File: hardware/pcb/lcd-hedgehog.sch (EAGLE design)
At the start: 22 parts

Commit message: added ble
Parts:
- added U$6: BLE113-A, jnode:BLE113-A
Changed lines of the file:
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@@
 <part name="U$4" library="HedgehogLib" deviceset="SFV23" device=""/>
 <part name="U$5" library="HedgehogLib" deviceset="LM2703" device=""/>
+<part name="U$6" library="jnode" deviceset="BLE113-A" device=""/>
 </parts>
 <sheets>
@@
 <instance part="U$4" gate="G$1" x="233.68" y="180.34"/>
 <instance part="U$5" gate="G$1" x="233.68" y="223.52"/>
+<instance part="U$6" gate="G$1" x="76.2" y="172.72"/>
 </instances>
 <busses>

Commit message: added some wiring
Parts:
- removed C_UC_P28/29, C_UC_P7/8: 0.22u, rcl:C-EUC0603K
- removed U$2: LSM303LGA28_LONG, jnode:LSM303LGA28_LONG
- added CC_DEBUGER: PROGCON, HedgehogLib:PROGCON
- added C_PWR_SW1, C_PWR_SW2: 10u, rcl:C-EUC0805K
- added HWB, RESET: (no value), jumper:SJ
- added R1: 10k, rcl:R-EU_R0603
- added R5, R6: 22, rcl:R-EU_R0603
- added U$7: LSM9D, jnode:LSM9D
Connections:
- removed net USB_D+@RC5: USB_CON.3
- removed net USB_D-@RC4: USB_CON.2
- new net BLE_RESET: CC_DEBUGER-2.S, U$6.RESET#
- new net CS_SD: U$1.(PCINT4/ADC11)PB4
- new net D+: R5.2, USB_CON.3
- new net D-: R6.2, USB_CON.2
- new net MISO: U$1.(PDO/PCINT3/MISO)PB3
- new net MOSI: U$1.(PDI/PCINT2/MOSI)PB2
- new net N$1: R1.1, RESET.2, U$1.RESET
- new net N$11: U$1.(PCINT6/OC1B/OC4B/ADC13)PB6
- new net N$2: 12MHZ_RESONATOR.2, U$1.XTAL1
- new net N$3: 12MHZ_RESONATOR.1, U$1.XTAL2
- new net N$4: HWB.1, U$1.(HWB)PE2
- new net N$5: R6.1, U$1.D-
- new net N$6: R5.1, U$1.D+
- new net N$7: U$7.SDA
- new net P0_1/INT: U$1.(PCINT5/OC1A/OC4B/ADC12)PB5, U$6.P0_1
- new net P0_4/TX: U$1.(RXD1/INT2)PD2, U$6.P0_4
- new net P0_5/RX: U$1.(TXD1/INT3)PD3, U$6.P0_5
- new net P2_1: CC_DEBUGER-4.S, U$6.P2_1
- new net P2_2: CC_DEBUGER-3.S, U$6.P2_2
- new net SCL: U$1.(OSC0B/SCL/INT0)PD0, U$3.SCL
- new net SDA: U$1.(SDA/INT1)PD1, U$3.SDA
- net +3V3: now also CC_DEBUGER-1.S, C_PWR_SW1.2, C_PWR_SW2.2, R1.2, U$1.AVCC, U$1.AVCC2, U$1.VCC, U$1.VCC2, U$3.VCC, U$6.AVDD, U$6.DVDD; no longer C_UC_P28/29.1, C_UC_P7/8.1
- net GND: now also CC_DEBUGER-5.S, C_PWR_SW1.1, C_PWR_SW2.1, HWB.2, RESET.1, U$1.GND, U$1.GND2, U$1.GND3, U$1.GND4, U$1.GND5, U$1.UCAP, U$1.UGND, U$3.VSS, U$4.VSS, U$5.GND, U$6.GND@1, U$6.GND@10, U$6.GND@11, U$6.GND@2, U$6.GND@3, U$6.GND@4, U$6.GND@5, U$6.GND@6, U$6.GND@8, U$6.GND@9, U$7.GND@1; no longer C_UC_P28/29.2, C_UC_P7/8.2
- net SCLK: now also U$1.(PCINT1/SCLK)PB1
- net V_USB: now also U$1.UVCC, U$1.VBUS
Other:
- note added: "I²C"
- note removed: "pin28&29"
- note removed: "pin37"
- note removed: "pin7&8"
- moved on the sheet: C_UC_P37, U$1

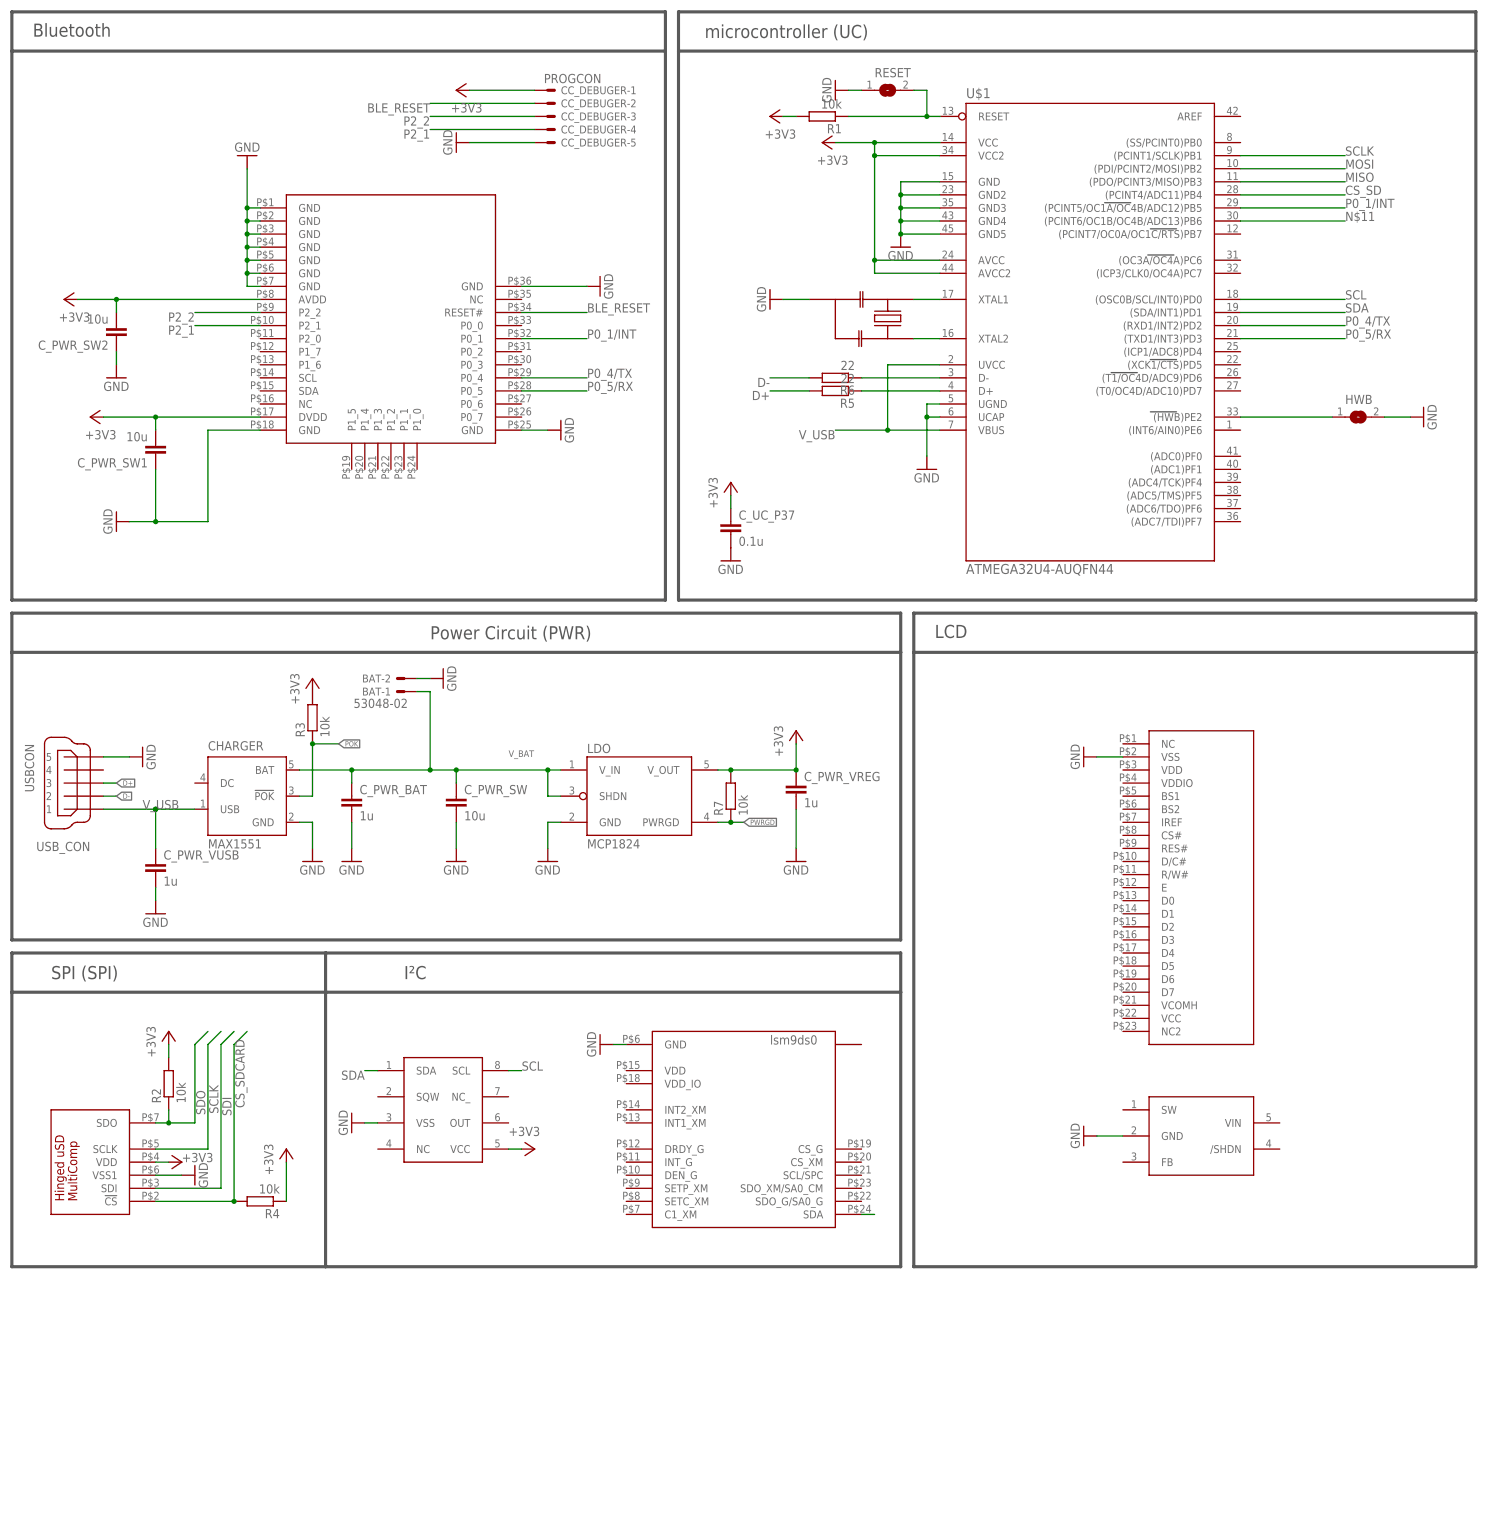
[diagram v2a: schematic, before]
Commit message: connected IMU
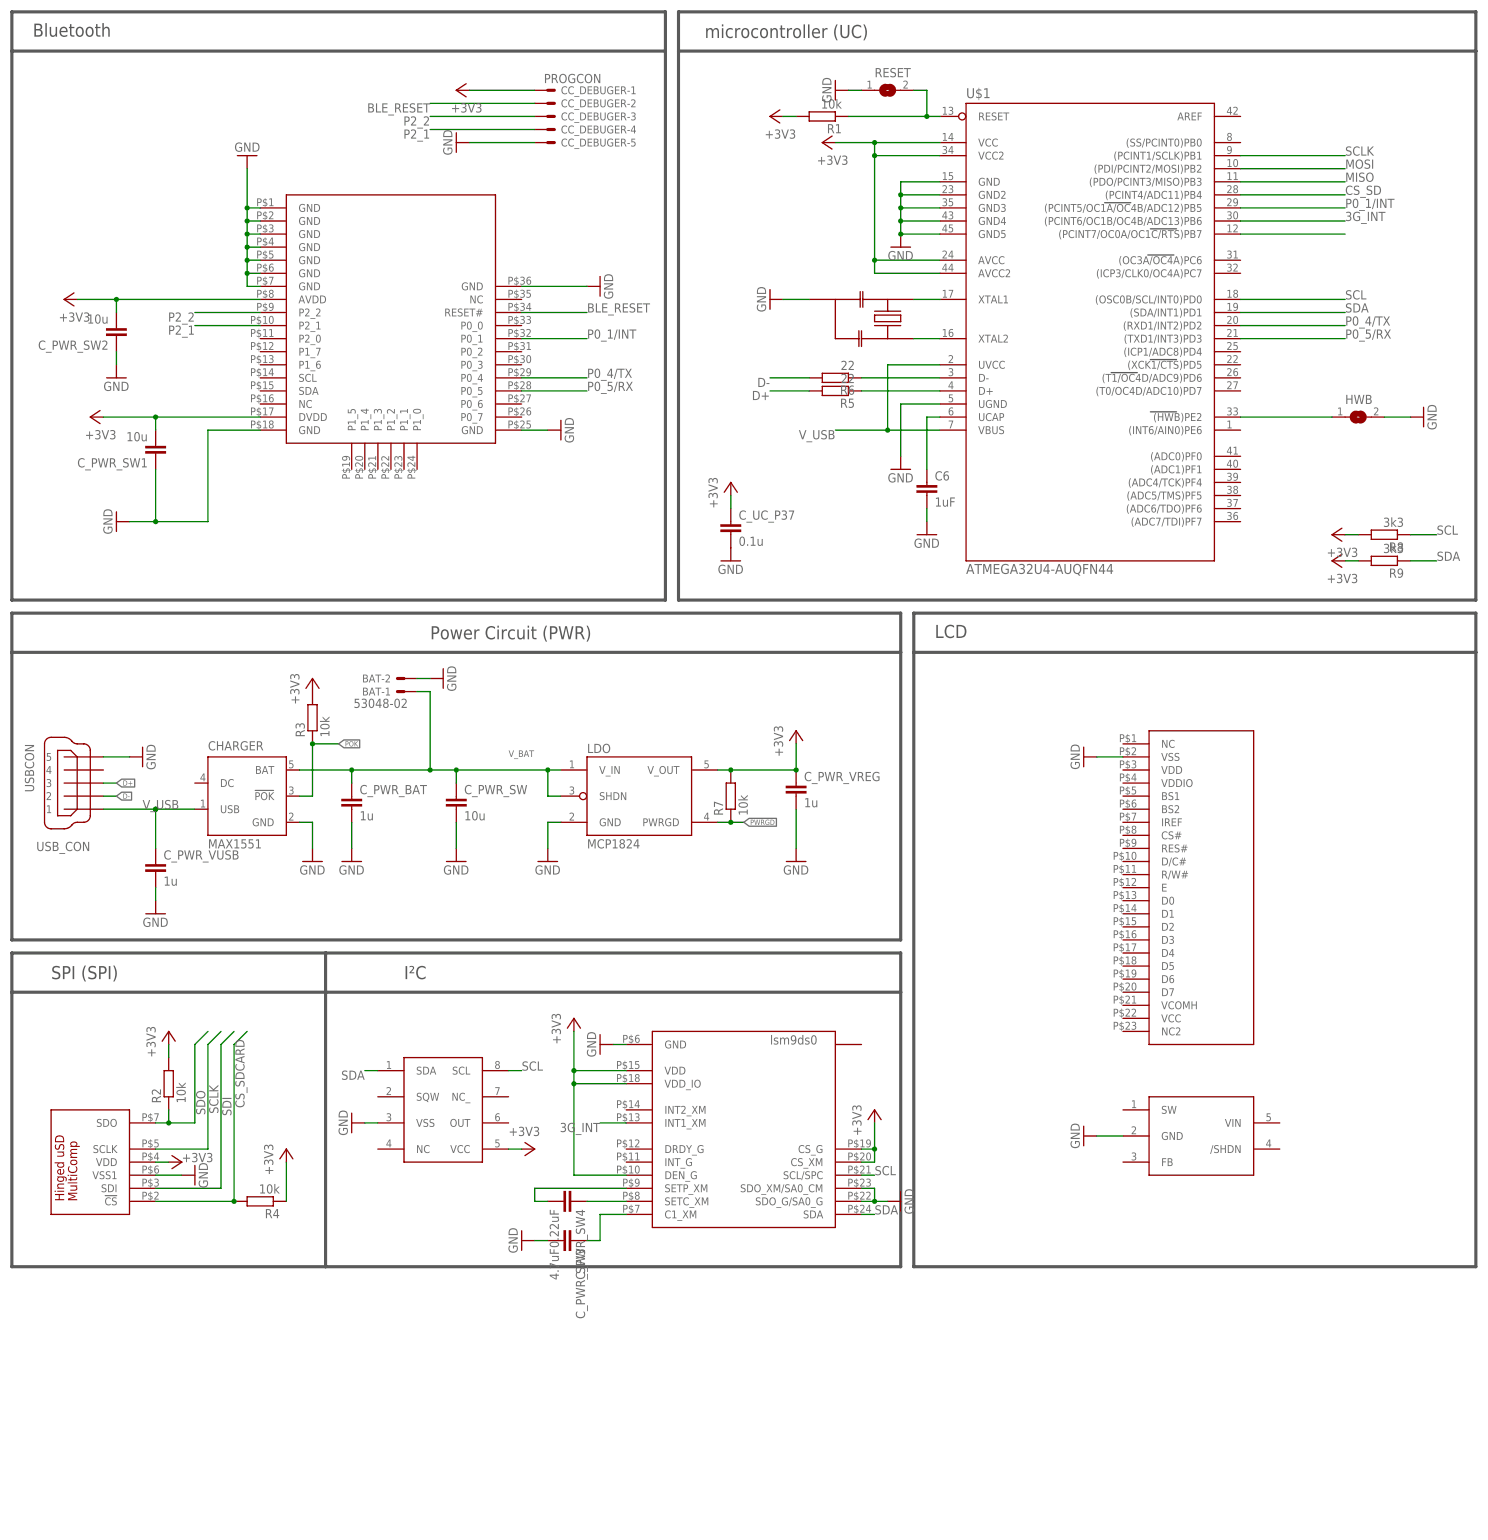
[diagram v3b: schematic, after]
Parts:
- added C6: 1uF, rcl:C-EUC0603K
- added C_PWR_SW3: 4.7uF, rcl:C-EUC0805K
- added C_PWR_SW4: 0.22uF, rcl:C-EUC0805K
- added R8, R9: 3k3, rcl:R-EU_R0603
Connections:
- new net 3G_INT: U$1.(PCINT6/OC1B/OC4B/ADC13)PB6, U$7.INT1_XM
- new net N$10: U$1.(PCINT7/OC0A/OC1C/RTS)PB7
- new net N$8: C_PWR_SW4.2, U$7.SETP_XM
- new net N$9: C_PWR_SW3.1, U$7.C1_XM
- net +3V3: now also R8.2, R9.2, U$7.CS_G, U$7.CS_XM, U$7.DEN_G, U$7.VDD, U$7.VDD_IO
- net GND: now also C6.2, C_PWR_SW3.2, U$7.SDO_G/SA0_G, U$7.SDO_XM/SA0_CM; no longer U$1.UCAP
- net N$11: now also C6.1, U$1.UCAP; no longer U$1.(PCINT6/OC1B/OC4B/ADC13)PB6
- net N$7: now also C_PWR_SW4.1, U$7.SETC_XM; no longer U$7.SDA
- net SCL: now also R8.1, U$7.SCL/SPC
- net SDA: now also R9.1, U$7.SDA
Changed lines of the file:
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@@
 <part name="+3V9" library="supply1" deviceset="+3V3" device=""/>
 <part name="GND18" library="supply1" deviceset="GND" device=""/>
+<part name="+3V12" library="supply1" deviceset="+3V3" device=""/>
+<part name="+3V13" library="supply1" deviceset="+3V3" device=""/>
+<part name="GND19" library="supply1" deviceset="GND" device=""/>
+<part name="C_PWR_SW3" library="rcl" deviceset="C-EU" device="C0805K" value="4.7uF"/>
+<part name="C_PWR_SW4" library="rcl" deviceset="C-EU" device="C0805K" value="0.22uF"/>
+<part name="GND22" library="supply1" deviceset="GND" device=""/>
+<part name="C6" library="rcl" deviceset="C-EU" device="C0603K" value="1uF"/>
+<part name="GND26" library="supply1" deviceset="GND" device=""/>
+<part name="R8" library="rcl" deviceset="R-EU_" device="R0603" value="3k3"/>
+<part name="+3V14" library="supply1" deviceset="+3V3" device=""/>
+<part name="R9" library="rcl" deviceset="R-EU_" device="R0603" value="3k3"/>
+<part name="+3V15" library="supply1" deviceset="+3V3" device=""/>
 </parts>
 <sheets>
@@
 <instance part="R1" gate="G$1" x="160.02" y="226.06" rot="R180"/>
 <instance part="+3V6" gate="G$1" x="149.86" y="226.06" rot="R90"/>
-<instance part="GND10" gate="1" x="180.34" y="157.48"/>
+<instance part="GND10" gate="1" x="175.26" y="157.48"/>
 <instance part="RESET" gate="1" x="172.72" y="231.14"/>
 <instance part="GND11" gate="1" x="162.56" y="231.14" rot="R270"/>
@@
 <instance part="+3V9" gate="G$1" x="104.14" y="25.4" rot="R270"/>
 <instance part="GND18" gate="1" x="116.84" y="45.72" rot="R270"/>
+<instance part="+3V12" gate="G$1" x="111.76" y="50.8"/>
+<instance part="+3V13" gate="G$1" x="170.18" y="33.02"/>
+<instance part="GND19" gate="1" x="175.26" y="15.24" rot="R90"/>
+<instance part="C_PWR_SW3" gate="G$1" x="111.76" y="7.62" rot="R270"/>
+<instance part="C_PWR_SW4" gate="G$1" x="111.76" y="15.24" rot="R270"/>
+<instance part="GND22" gate="1" x="101.6" y="7.62" rot="R270"/>
+<instance part="C6" gate="G$1" x="180.34" y="154.94"/>
+<instance part="GND26" gate="1" x="180.34" y="144.78"/>
+<instance part="R8" gate="G$1" x="269.24" y="144.78" rot="R180"/>
+<instance part="+3V14" gate="G$1" x="259.08" y="144.78" rot="R90"/>
+<instance part="R9" gate="G$1" x="269.24" y="139.7" rot="R180"/>
+<instance part="+3V15" gate="G$1" x="259.08" y="139.7" rot="R90"/>
 </instances>
 <busses>
@@
 </segment>
 <segment>
-<pinref part="U$1" gate="G$1" pin="UCAP"/>
-<wire x1="182.88" y1="167.64" x2="180.34" y2="167.64" width="0.1524" layer="91"/>
 <pinref part="GND10" gate="1" pin="GND"/>
-<wire x1="180.34" y1="160.02" x2="180.34" y2="167.64" width="0.1524" layer="91"/>
+<wire x1="175.26" y1="160.02" x2="175.26" y2="170.18" width="0.1524" layer="91"/>
 <pinref part="U$1" gate="G$1" pin="UGND"/>
-<wire x1="182.88" y1="170.18" x2="180.34" y2="170.18" width="0.1524" layer="91"/>
-<wire x1="180.34" y1="170.18" x2="180.34" y2="167.64" width="0.1524" layer="91"/>
-<junction x="180.34" y="167.64"/>
+<wire x1="182.88" y1="170.18" x2="175.26" y2="170.18" width="0.1524" layer="91"/>
 </segment>
 <segment>
@@
 <pinref part="GND18" gate="1" pin="GND"/>
 <wire x1="119.38" y1="45.72" x2="121.92" y2="45.72" width="0.1524" layer="91"/>
+</segment>
+<segment>
+<pinref part="U$7" gate="G$1" pin="SDO_G/SA0_G"/>
+<pinref part="GND19" gate="1" pin="GND"/>
+<wire x1="172.72" y1="15.24" x2="170.18" y2="15.24" width="0.1524" layer="91"/>
+<pinref part="U$7" gate="G$1" pin="SDO_XM/SA0_CM"/>
+<wire x1="170.18" y1="15.24" x2="167.64" y2="15.24" width="0.1524" layer="91"/>
+<wire x1="167.64" y1="17.78" x2="170.18" y2="17.78" width="0.1524" layer="91"/>
+<wire x1="170.18" y1="17.78" x2="170.18" y2="15.24" width="0.1524" layer="91"/>
+<junction x="170.18" y="15.24"/>
+</segment>
+<segment>
+<pinref part="C_PWR_SW3" gate="G$1" pin="2"/>
+<pinref part="GND22" gate="1" pin="GND"/>
+<wire x1="104.14" y1="7.62" x2="106.68" y2="7.62" width="0.1524" layer="91"/>
+</segment>
+<segment>
+<pinref part="C6" gate="G$1" pin="2"/>
+<pinref part="GND26" gate="1" pin="GND"/>
+<wire x1="180.34" y1="147.32" x2="180.34" y2="149.86" width="0.1524" layer="91"/>
 </segment>
 </net>
@@
 <wire x1="99.06" y1="25.4" x2="101.6" y2="25.4" width="0.1524" layer="91"/>
 <pinref part="+3V9" gate="G$1" pin="+3V3"/>
+</segment>
+<segment>
+<pinref part="U$7" gate="G$1" pin="VDD"/>
+<pinref part="+3V12" gate="G$1" pin="+3V3"/>
+<wire x1="121.92" y1="40.64" x2="111.76" y2="40.64" width="0.1524" layer="91"/>
+<wire x1="111.76" y1="40.64" x2="111.76" y2="48.26" width="0.1524" layer="91"/>
+<pinref part="U$7" gate="G$1" pin="VDD_IO"/>
+<wire x1="121.92" y1="38.1" x2="111.76" y2="38.1" width="0.1524" layer="91"/>
+<wire x1="111.76" y1="38.1" x2="111.76" y2="40.64" width="0.1524" layer="91"/>
+<pinref part="U$7" gate="G$1" pin="DEN_G"/>
+<wire x1="121.92" y1="20.32" x2="111.76" y2="20.32" width="0.1524" layer="91"/>
+<wire x1="111.76" y1="20.32" x2="111.76" y2="38.1" width="0.1524" layer="91"/>
+<junction x="111.76" y="40.64"/>
+<junction x="111.76" y="38.1"/>
+</segment>
+<segment>
+<pinref part="U$7" gate="G$1" pin="CS_G"/>
+<wire x1="167.64" y1="25.4" x2="170.18" y2="25.4" width="0.1524" layer="91"/>
+<wire x1="170.18" y1="25.4" x2="170.18" y2="30.48" width="0.1524" layer="91"/>
+<pinref part="U$7" gate="G$1" pin="CS_XM"/>
+<wire x1="167.64" y1="22.86" x2="170.18" y2="22.86" width="0.1524" layer="91"/>
+<wire x1="170.18" y1="22.86" x2="170.18" y2="25.4" width="0.1524" layer="91"/>
+<pinref part="+3V13" gate="G$1" pin="+3V3"/>
+<junction x="170.18" y="25.4"/>
+</segment>
+<segment>
+<pinref part="+3V14" gate="G$1" pin="+3V3"/>
+<pinref part="R8" gate="G$1" pin="2"/>
+<wire x1="261.62" y1="144.78" x2="264.16" y2="144.78" width="0.1524" layer="91"/>
+</segment>
+<segment>
+<pinref part="+3V15" gate="G$1" pin="+3V3"/>
+<pinref part="R9" gate="G$1" pin="2"/>
+<wire x1="261.62" y1="139.7" x2="264.16" y2="139.7" width="0.1524" layer="91"/>
 </segment>
 </net>
@@
 <label x="71.12" y="40.64" size="1.778" layer="95" rot="R180"/>
 </segment>
+<segment>
+<pinref part="U$7" gate="G$1" pin="SDA"/>
+<wire x1="167.64" y1="12.7" x2="170.18" y2="12.7" width="0.1524" layer="91"/>
+<label x="170.18" y="12.7" size="1.778" layer="95"/>
+</segment>
+<segment>
+<pinref part="R9" gate="G$1" pin="1"/>
+<wire x1="274.32" y1="139.7" x2="279.4" y2="139.7" width="0.1524" layer="91"/>
+<label x="279.4" y="139.7" size="1.778" layer="95"/>
+</segment>
 </net>
 <net name="SCL" class="0">
@@
 <label x="101.6" y="40.64" size="1.778" layer="95"/>
 </segment>
+<segment>
+<pinref part="U$7" gate="G$1" pin="SCL/SPC"/>
+<wire x1="167.64" y1="20.32" x2="170.18" y2="20.32" width="0.1524" layer="91"/>
+<label x="170.18" y="20.32" size="1.778" layer="95"/>
+</segment>
+<segment>
+<pinref part="R8" gate="G$1" pin="1"/>
+<wire x1="274.32" y1="144.78" x2="279.4" y2="144.78" width="0.1524" layer="91"/>
+<label x="279.4" y="144.78" size="1.778" layer="95"/>
+</segment>
 </net>
 <net name="MOSI" class="0">
@@
 </segment>
 </net>
-<net name="N$11" class="0">
+<net name="CS_SD" class="0">
+<segment>
+<pinref part="U$1" gate="G$1" pin="(PCINT4/ADC11)PB4"/>
+<wire x1="241.3" y1="210.82" x2="261.62" y2="210.82" width="0.1524" layer="91"/>
+<label x="261.62" y="210.82" size="1.778" layer="95"/>
+</segment>
+</net>
+<net name="N$7" class="0">
+<segment>
+<pinref part="U$7" gate="G$1" pin="SETC_XM"/>
+<pinref part="C_PWR_SW4" gate="G$1" pin="1"/>
+<wire x1="121.92" y1="15.24" x2="114.3" y2="15.24" width="0.1524" layer="91"/>
+</segment>
+</net>
+<net name="N$8" class="0">
+<segment>
+<pinref part="C_PWR_SW4" gate="G$1" pin="2"/>
+<wire x1="106.68" y1="15.24" x2="104.14" y2="15.24" width="0.1524" layer="91"/>
+<wire x1="104.14" y1="15.24" x2="104.14" y2="17.78" width="0.1524" layer="91"/>
+<pinref part="U$7" gate="G$1" pin="SETP_XM"/>
+<wire x1="104.14" y1="17.78" x2="121.92" y2="17.78" width="0.1524" layer="91"/>
+</segment>
+</net>
+<net name="N$9" class="0">
+<segment>
+<pinref part="U$7" gate="G$1" pin="C1_XM"/>
+<wire x1="121.92" y1="12.7" x2="116.84" y2="12.7" width="0.1524" layer="91"/>
+<wire x1="116.84" y1="12.7" x2="116.84" y2="7.62" width="0.1524" layer="91"/>
+<pinref part="C_PWR_SW3" gate="G$1" pin="1"/>
+<wire x1="116.84" y1="7.62" x2="114.3" y2="7.62" width="0.1524" layer="91"/>
+</segment>
+</net>
+<net name="3G_INT" class="0">
 <segment>
 <pinref part="U$1" gate="G$1" pin="(PCINT6/OC1B/OC4B/ADC13)PB6"/>
@@
 <label x="261.62" y="205.74" size="1.778" layer="95"/>
 </segment>
-</net>
-<net name="CS_SD" class="0">
-<segment>
-<pinref part="U$1" gate="G$1" pin="(PCINT4/ADC11)PB4"/>
-<wire x1="241.3" y1="210.82" x2="261.62" y2="210.82" width="0.1524" layer="91"/>
-<label x="261.62" y="210.82" size="1.778" layer="95"/>
-</segment>
-</net>
-<net name="N$7" class="0">
-<segment>
-<pinref part="U$7" gate="G$1" pin="SDA"/>
-<wire x1="167.64" y1="12.7" x2="170.18" y2="12.7" width="0.1524" layer="91"/>
-</segment>
-</net>
+<segment>
+<pinref part="U$7" gate="G$1" pin="INT1_XM"/>
+<wire x1="121.92" y1="30.48" x2="116.84" y2="30.48" width="0.1524" layer="91"/>
+<label x="116.84" y="30.48" size="1.778" layer="95" rot="R180"/>
+</segment>
+</net>
+<net name="N$10" class="0">
+<segment>
+<pinref part="U$1" gate="G$1" pin="(PCINT7/OC0A/OC1C/RTS)PB7"/>
+<wire x1="241.3" y1="203.2" x2="261.62" y2="203.2" width="0.1524" layer="91"/>
+</segment>
+</net>
+<net name="N$11" class="0">
+<segment>
+<pinref part="U$1" gate="G$1" pin="UCAP"/>
+<wire x1="182.88" y1="167.64" x2="180.34" y2="167.64" width="0.1524" layer="91"/>
+<wire x1="180.34" y1="167.64" x2="180.34" y2="157.48" width="0.1524" layer="91"/>
+<pinref part="C6" gate="G$1" pin="1"/>
+</segment>
+</net>
